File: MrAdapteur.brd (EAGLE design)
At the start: 95 x 45.3 mm, 20 parts, among them X1 1751248

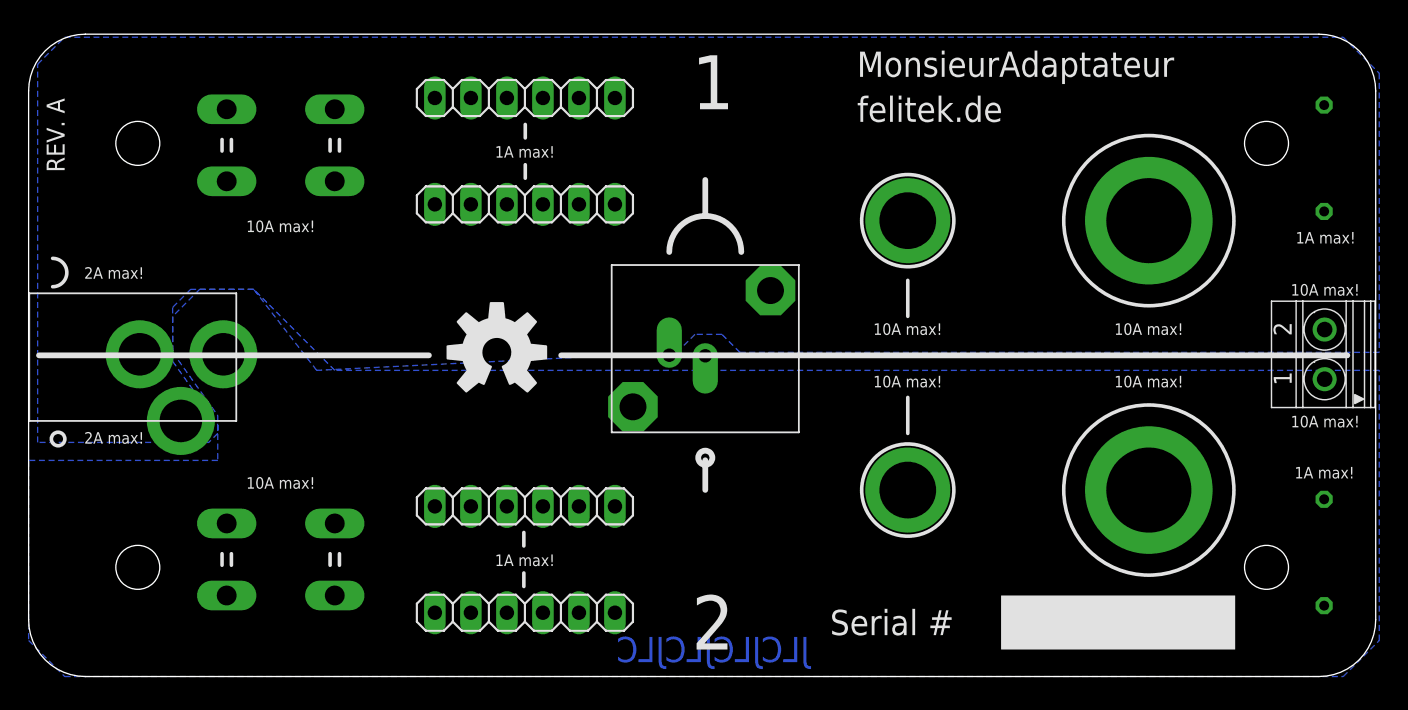
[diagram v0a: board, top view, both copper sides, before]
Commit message: Fixed hole size for wire clips, added stop mask for the UL/Manufacturing marks
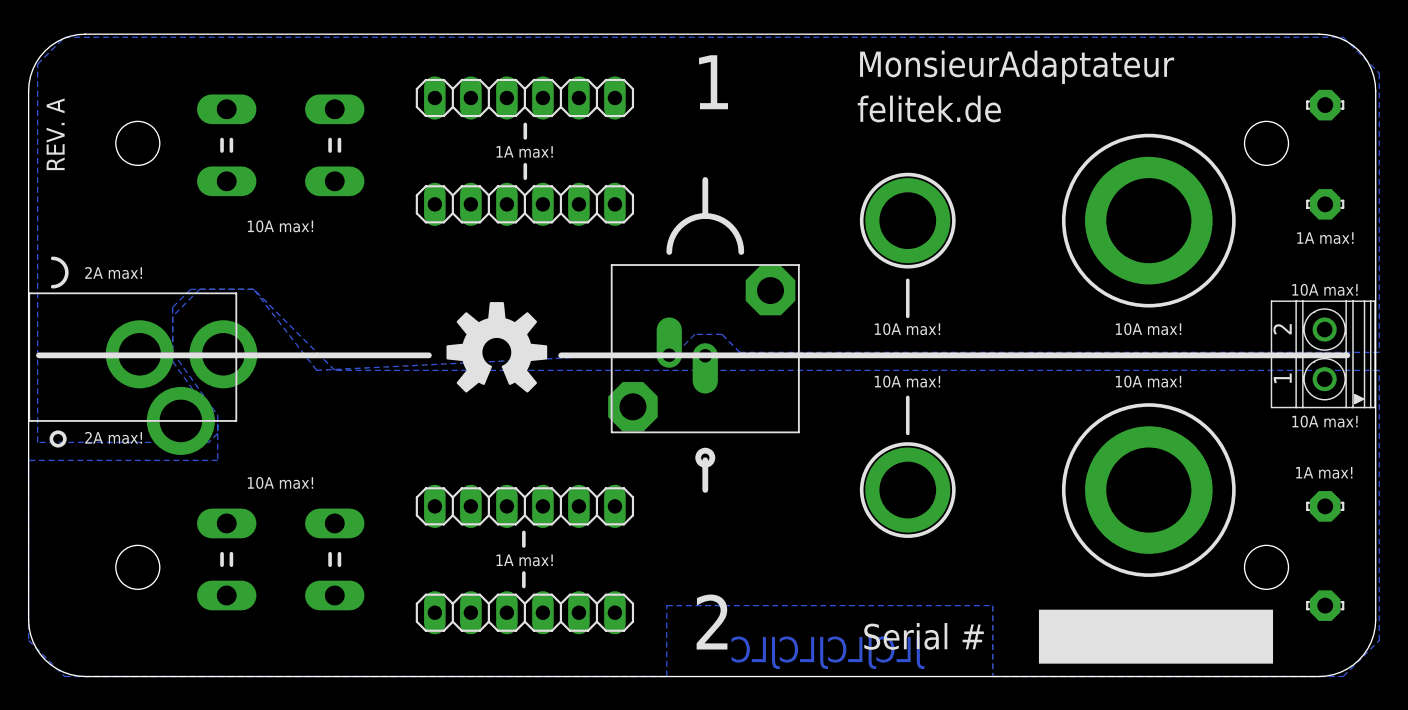
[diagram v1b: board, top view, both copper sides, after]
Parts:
- removed U$10, U$11, U$8, U$9: SOLPAD07, 4mm:SOLPAD07
- added LSP1, LSP2, LSP3, LSP4: LSP11, solpad:LSP11
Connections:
- net N$1: now also LSP1.MP, LSP2.MP; no longer U$10.P$1, U$8.P$1
- net N$3: now also LSP3.MP, LSP4.MP; no longer U$11.P$1, U$9.P$1
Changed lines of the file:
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@@
 <setting verticaltext="up"/>
 </settings>
-<grid distance="1.27" unitdist="mm" unit="mm" style="lines" multiple="1" display="no" altdistance="0.025" altunitdist="inch" altunit="inch"/>
+<grid distance="1" unitdist="mm" unit="mm" style="lines" multiple="1" display="no" altdistance="0.25" altunitdist="mm" altunit="mm"/>
 <layers>
 <layer number="1" name="Top" color="4" fill="1" visible="yes" active="yes"/>
@@
 <layer number="14" name="Route14" color="1" fill="6" visible="no" active="no"/>
 <layer number="15" name="Route15" color="4" fill="6" visible="no" active="no"/>
-<layer number="16" name="Bottom" color="1" fill="1" visible="no" active="yes"/>
+<layer number="16" name="Bottom" color="1" fill="1" visible="yes" active="yes"/>
 <layer number="17" name="Pads" color="2" fill="1" visible="yes" active="yes"/>
 <layer number="18" name="Vias" color="2" fill="1" visible="yes" active="yes"/>
@@
 <layer number="20" name="Dimension" color="15" fill="1" visible="yes" active="yes"/>
 <layer number="21" name="tPlace" color="7" fill="1" visible="yes" active="yes"/>
-<layer number="22" name="bPlace" color="7" fill="1" visible="no" active="yes"/>
+<layer number="22" name="bPlace" color="7" fill="1" visible="yes" active="yes"/>
 <layer number="23" name="tOrigins" color="15" fill="1" visible="yes" active="yes"/>
-<layer number="24" name="bOrigins" color="15" fill="1" visible="no" active="yes"/>
+<layer number="24" name="bOrigins" color="15" fill="1" visible="yes" active="yes"/>
 <layer number="25" name="tNames" color="7" fill="1" visible="yes" active="yes"/>
-<layer number="26" name="bNames" color="7" fill="1" visible="no" active="yes"/>
+<layer number="26" name="bNames" color="7" fill="1" visible="yes" active="yes"/>
 <layer number="27" name="tValues" color="7" fill="1" visible="yes" active="yes"/>
-<layer number="28" name="bValues" color="7" fill="1" visible="no" active="yes"/>
-<layer number="29" name="tStop" color="7" fill="3" visible="no" active="yes"/>
-<layer number="30" name="bStop" color="7" fill="6" visible="no" active="yes"/>
+<layer number="28" name="bValues" color="7" fill="1" visible="yes" active="yes"/>
+<layer number="29" name="tStop" color="7" fill="3" visible="yes" active="yes"/>
+<layer number="30" name="bStop" color="7" fill="6" visible="yes" active="yes"/>
 <layer number="31" name="tCream" color="7" fill="4" visible="no" active="yes"/>
 <layer number="32" name="bCream" color="7" fill="5" visible="no" active="yes"/>
@@
 <text x="17.78" y="31.75" size="0.8128" layer="25" align="center">10A max!</text>
 <text x="17.78" y="13.6525" size="0.8128" layer="25" align="center">10A max!</text>
-<text x="91.47" y="30.945" size="0.8128" layer="25" rot="R180" align="center">1A max!</text>
+<text x="91.47" y="30.925" size="0.8128" layer="25" rot="R180" align="center">1A max!</text>
 <text x="6.0325" y="16.8275" size="0.8128" layer="25" align="center">2A max!</text>
 <text x="91.44" y="27.27" size="0.8128" layer="25" rot="R180" align="center">10A max!</text>
@@
 <wire x1="62" y1="17.145" x2="62" y2="19.685" width="0.254" layer="25"/>
 <wire x1="0.73" y1="22.65" x2="28.23" y2="22.65" width="0.4064" layer="25"/>
-<text x="48.26" y="1.905" size="1.778" layer="16" rot="MR0" align="center">JLCJLCJLCJLC</text>
+<text x="56.26" y="1.905" size="1.778" layer="16" rot="MR0" align="center">JLCJLCJLCJLC</text>
 <text x="2.54" y="35.56" size="1.27" layer="25" rot="R90">REV. A</text>
-<rectangle x1="68.58" y1="1.905" x2="85.09" y2="5.715" layer="25"/>
-<text x="56.515" y="3.81" size="1.778" layer="25" align="center-left">Serial #</text>
+<rectangle x1="71.25" y1="0.905" x2="87.76" y2="4.715" layer="25"/>
+<text x="58.785" y="2.81" size="1.778" layer="25" align="center-left">Serial #</text>
+<polygon width="0.4064" layer="30">
+<vertex x="45.75" y="4.25"/>
+<vertex x="45.75" y="0"/>
+<vertex x="67.25" y="0"/>
+<vertex x="67.25" y="4.25"/>
+</polygon>
 </plain>
 <attributes>
@@
 </element>
 <element name="U$7" library="SparkFun" package="OSHW-LOGO-L" value="" x="33.02" y="22.86"/>
-<element name="U$8" library="4mm" package="SOLPAD07" value="SOLPAD07" x="91.365" y="5"/>
-<element name="U$9" library="4mm" package="SOLPAD07" value="SOLPAD07" x="91.365" y="40.3"/>
-<element name="U$10" library="4mm" package="SOLPAD07" value="SOLPAD07" x="91.365" y="12.5"/>
-<element name="U$11" library="4mm" package="SOLPAD07" value="SOLPAD07" x="91.365" y="32.8"/>
+<element name="LSP1" library="solpad" package="LSP11" value="LSP11" x="91.44" y="5" smashed="yes">
+<attribute name="VALUE" x="91.44" y="5.254" size="0.0254" layer="27"/>
+</element>
+<element name="LSP2" library="solpad" package="LSP11" value="LSP11" x="91.44" y="12" smashed="yes">
+<attribute name="VALUE" x="91.44" y="12.254" size="0.0254" layer="27"/>
+</element>
+<element name="LSP3" library="solpad" package="LSP11" value="LSP11" x="91.44" y="40.3" smashed="yes">
+<attribute name="VALUE" x="91.44" y="40.554" size="0.0254" layer="27"/>
+</element>
+<element name="LSP4" library="solpad" package="LSP11" value="LSP11" x="91.44" y="33.3" smashed="yes">
+<attribute name="VALUE" x="91.44" y="33.554" size="0.0254" layer="27"/>
+</element>
 </elements>
 <signals>
@@
 <vertex x="0" y="2.54"/>
 <vertex x="2.54" y="0"/>
+<vertex x="45" y="0"/>
+<vertex x="45" y="5"/>
+<vertex x="68" y="5"/>
+<vertex x="68" y="0"/>
 <vertex x="92.71" y="0"/>
 <vertex x="95.25" y="2.54"/>
 </polygon>
 <contactref element="U$6" pad="TIP"/>
-<contactref element="U$8" pad="P$1"/>
-<contactref element="U$10" pad="P$1"/>
+<contactref element="LSP2" pad="MP"/>
+<contactref element="LSP1" pad="MP"/>
 </signal>
 <signal name="N$3">
@@
 <contactref element="U$6" pad="RING"/>
 <contactref element="U$6" pad="RING_SW"/>
-<contactref element="U$9" pad="P$1"/>
-<contactref element="U$11" pad="P$1"/>
+<contactref element="LSP3" pad="MP"/>
+<contactref element="LSP4" pad="MP"/>
 </signal>
 </signals>
